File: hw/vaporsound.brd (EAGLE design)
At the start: 100 x 80 mm, 83 parts, among them P9 MA23-2, Q1 BSS138, Q2 BSS138

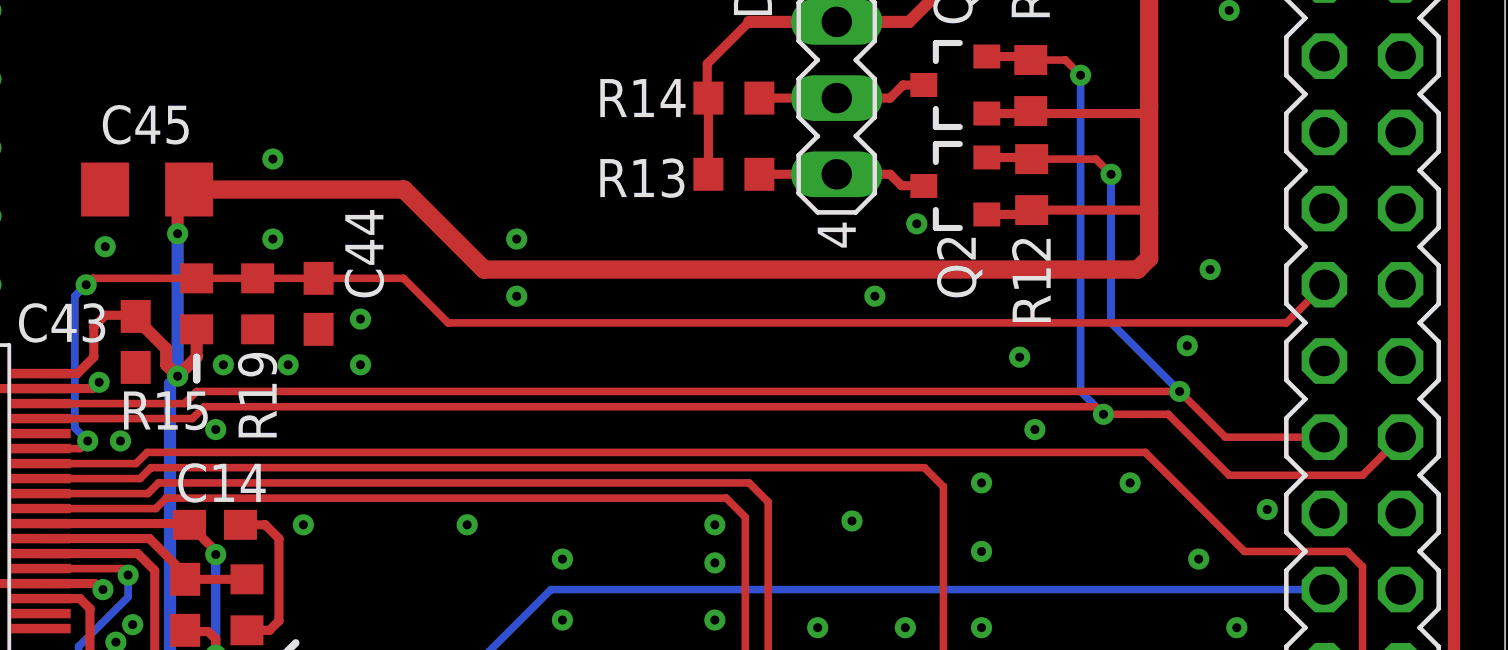
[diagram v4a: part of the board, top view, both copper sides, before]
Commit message: move reset to different bbb pin and remove pull-down resistor
reset of the sta350 is now connected to a pin with pull-up on the bbb instead of one with a pull-down
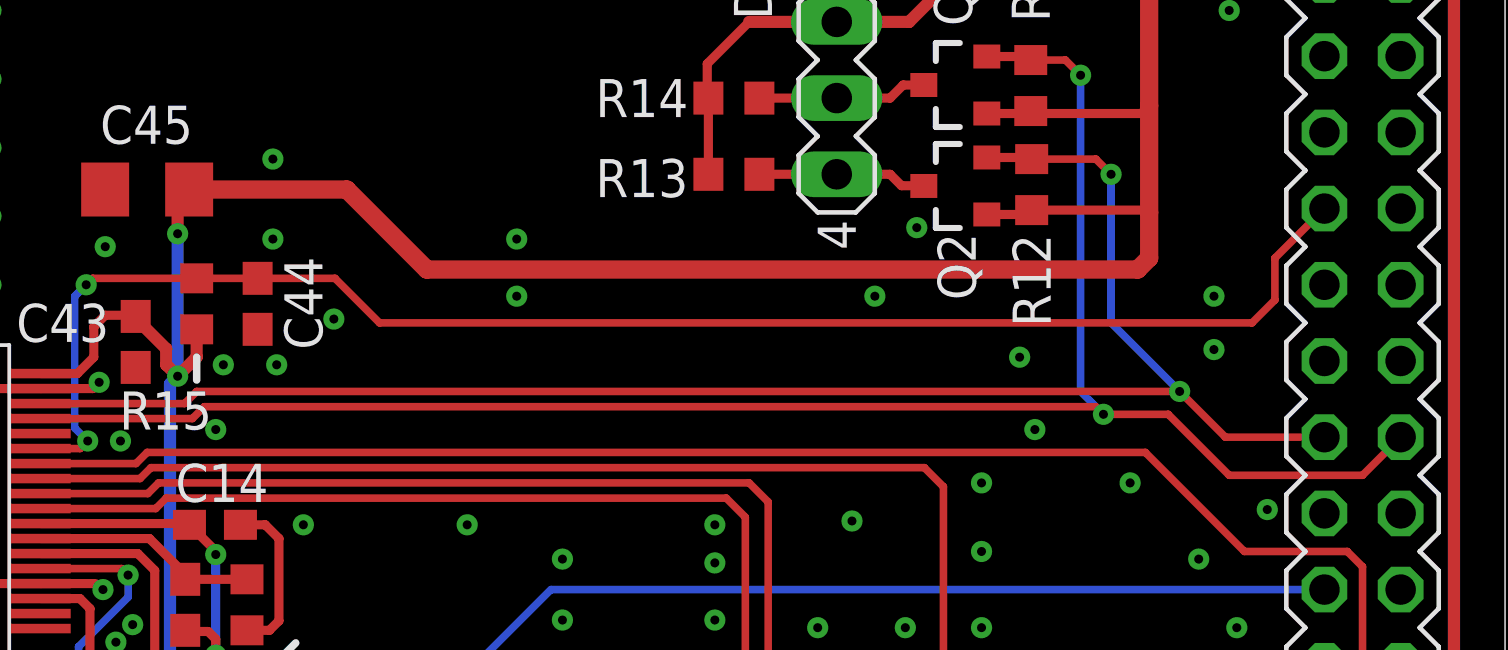
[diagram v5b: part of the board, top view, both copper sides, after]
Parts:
- removed R19: DNP, rcl:R0603
- moved C44 2.03 mm to (58.4, 46.4)
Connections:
- net GND: no longer R19.1
- net RESET: now also P9.13; no longer P9.15, R19.2
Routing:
- net RESET: track 49.8 -> 51.6 mm
- net GND: vias 546 -> 545
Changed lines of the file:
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@@
 <attribute name="VALUE" x="54.483" y="46.99" size="1.27" layer="27" rot="R270"/>
 </element>
-<element name="C44" library="rcl" package="C0603" value="1n" x="60.452" y="46.355" smashed="yes" rot="R270">
-<attribute name="NAME" x="62.611" y="46.482" size="1.27" layer="25" font="vector" ratio="14" rot="R90"/>
-<attribute name="VALUE" x="58.547" y="46.99" size="1.27" layer="27" rot="R270"/>
+<element name="C44" library="rcl" package="C0603" value="1n" x="58.42" y="46.355" smashed="yes" rot="R270">
+<attribute name="NAME" x="60.579" y="44.831" size="1.27" layer="25" font="vector" ratio="14" rot="R90"/>
+<attribute name="VALUE" x="56.515" y="46.99" size="1.27" layer="27" rot="R270"/>
 </element>
 <element name="C45" library="rcl" package="C1206" value="22u" x="54.737" y="50.165" smashed="yes" rot="R180">
@@
 <attribute name="NAME" x="52.0192" y="24.9174" size="1.27" layer="25" font="vector" ratio="14"/>
 <attribute name="VALUE" x="52.9336" y="25.4" size="1.27" layer="27"/>
-</element>
-<element name="R19" library="rcl" package="R0603" value="DNP" x="58.42" y="46.355" smashed="yes" rot="R90">
-<attribute name="NAME" x="57.785" y="44.831" size="1.27" layer="25" font="vector" ratio="14" rot="R270"/>
-<attribute name="VALUE" x="60.325" y="45.72" size="1.27" layer="27" rot="R90"/>
 </element>
 <element name="L1" library="custom-ind" package="SRR1210" value="" x="27.178" y="26.416" smashed="yes">
@@
 <via x="84.328" y="42.164" extent="1-16" drill="0.3"/>
 <via x="57.277" y="44.323" extent="1-16" drill="0.3"/>
-<via x="59.436" y="44.323" extent="1-16" drill="0.3"/>
+<via x="59.055" y="44.323" extent="1-16" drill="0.3"/>
 <via x="83.82" y="44.577" extent="1-16" drill="0.3"/>
-<via x="89.408" y="44.958" extent="1-16" drill="0.3"/>
+<via x="90.297" y="44.831" extent="1-16" drill="0.3"/>
 <via x="80.01" y="28.829" extent="1-16" drill="0.3"/>
 <via x="77.089" y="29.845" extent="1-16" drill="0.3"/>
@@
 <via x="58.928" y="48.514" extent="1-16" drill="0.3"/>
 <via x="78.994" y="46.609" extent="1-16" drill="0.3"/>
-<via x="90.17" y="47.498" extent="1-16" drill="0.3"/>
+<via x="90.297" y="46.609" extent="1-16" drill="0.3"/>
 <via x="82.55" y="32.512" extent="1-16" drill="0.3"/>
 <via x="65.405" y="38.989" extent="1-16" drill="0.3"/>
@@
 <via x="73.66" y="38.989" extent="1-16" drill="0.3"/>
 <contactref element="R18" pad="2"/>
-<contactref element="R19" pad="1"/>
 <via x="78.232" y="39.116" extent="1-16" drill="0.3"/>
 <via x="82.55" y="38.1" extent="1-16" drill="0.3"/>
@@
 <via x="77.724" y="27.2542" extent="1-16" drill="0.3"/>
 <via x="74.168" y="24.003" extent="1-16" drill="0.3"/>
-<via x="61.849" y="44.323" extent="1-16" drill="0.3"/>
 <via x="53.34" y="48.26" extent="1-16" drill="0.3"/>
 <via x="79.121" y="16.002" extent="1-16" drill="0.3"/>
@@
 <via x="88.265" y="29.9974" extent="1-16" drill="0.3"/>
 <via x="58.928" y="51.181" extent="1-16" drill="0.3"/>
-<via x="80.391" y="49.022" extent="1-16" drill="0.3"/>
+<via x="80.391" y="48.895" extent="1-16" drill="0.3"/>
 <via x="20.574" y="67.437" extent="1-16" drill="0.3"/>
 <via x="20.574" y="11.938" extent="1-16" drill="0.3"/>
-<via x="61.849" y="45.847" extent="1-16" drill="0.3"/>
+<via x="60.96" y="45.847" extent="1-16" drill="0.3"/>
 <via x="67.056" y="48.514" extent="1-16" drill="0.3"/>
 <via x="67.056" y="46.609" extent="1-16" drill="0.3"/>
@@
 <wire x1="84.222" y1="49.479" x2="88.062" y2="49.479" width="0.3048" layer="1"/>
 <wire x1="88.062" y1="49.479" x2="88.138" y2="49.403" width="0.3048" layer="1"/>
-<wire x1="65.9638" y1="47.498" x2="87.757" y2="47.498" width="0.6096" layer="1"/>
+<wire x1="64.0588" y1="47.498" x2="87.757" y2="47.498" width="0.6096" layer="1"/>
 <wire x1="87.757" y1="47.498" x2="88.138" y2="47.879" width="0.6096" layer="1"/>
 <wire x1="88.138" y1="47.879" x2="88.138" y2="49.403" width="0.6096" layer="1"/>
@@
 <wire x1="53.34" y1="45.974" x2="54.317" y2="45.974" width="0.3048" layer="1"/>
 <wire x1="54.317" y1="45.974" x2="54.356" y2="45.935" width="0.3048" layer="1"/>
-<wire x1="65.9638" y1="47.498" x2="63.2968" y2="50.165" width="0.6096" layer="1"/>
-<wire x1="56.137" y1="50.165" x2="63.2968" y2="50.165" width="0.6096" layer="1"/>
+<wire x1="64.0588" y1="47.498" x2="61.3918" y2="50.165" width="0.6096" layer="1"/>
+<wire x1="56.137" y1="50.165" x2="61.3918" y2="50.165" width="0.6096" layer="1"/>
 <wire x1="53.848" y1="30.734" x2="52.7694" y2="30.734" width="0.3048" layer="1"/>
 <wire x1="52.7694" y1="30.734" x2="52.7304" y2="30.695" width="0.3048" layer="1"/>
@@
 <signal name="RESET">
 <contactref element="U$1" pad="P$31"/>
-<contactref element="P9" pad="15"/>
 <wire x1="51.191" y1="41.53" x2="52.5028" y2="41.53" width="0.254" layer="1"/>
 <wire x1="52.5028" y1="41.53" x2="52.7558" y2="41.783" width="0.254" layer="1"/>
@@
 <wire x1="52.324" y1="46.609" x2="52.705" y2="46.99" width="0.254" layer="16"/>
 <via x="52.705" y="46.99" extent="1-16" drill="0.3"/>
-<wire x1="64.77" y1="45.72" x2="63.285" y2="47.205" width="0.254" layer="1"/>
-<wire x1="64.77" y1="45.72" x2="92.71" y2="45.72" width="0.254" layer="1"/>
-<wire x1="92.71" y1="45.72" x2="93.98" y2="46.99" width="0.254" layer="1"/>
+<wire x1="62.484" y1="45.72" x2="60.999" y2="47.205" width="0.254" layer="1"/>
+<wire x1="62.484" y1="45.72" x2="91.567" y2="45.72" width="0.254" layer="1"/>
 <contactref element="C44" pad="1"/>
 <contactref element="R15" pad="1"/>
-<contactref element="R19" pad="2"/>
-<wire x1="58.42" y1="47.244" x2="58.42" y2="47.205" width="0.4064" layer="1"/>
-<wire x1="58.42" y1="47.205" x2="60.452" y2="47.205" width="0.254" layer="1"/>
-<wire x1="60.452" y1="47.205" x2="63.285" y2="47.205" width="0.254" layer="1"/>
+<wire x1="58.42" y1="47.205" x2="60.999" y2="47.205" width="0.254" layer="1"/>
 <wire x1="52.705" y1="46.99" x2="52.92" y2="47.205" width="0.254" layer="1"/>
 <wire x1="52.92" y1="47.205" x2="56.388" y2="47.205" width="0.254" layer="1"/>
 <wire x1="56.388" y1="47.205" x2="58.42" y2="47.205" width="0.254" layer="1"/>
+<contactref element="P9" pad="13"/>
+<wire x1="93.98" y1="49.53" x2="92.329" y2="47.879" width="0.254" layer="1"/>
+<wire x1="92.329" y1="47.879" x2="92.329" y2="46.482" width="0.254" layer="1"/>
+<wire x1="92.329" y1="46.482" x2="91.567" y2="45.72" width="0.254" layer="1"/>
 </signal>
 <signal name="POWERDOWN">

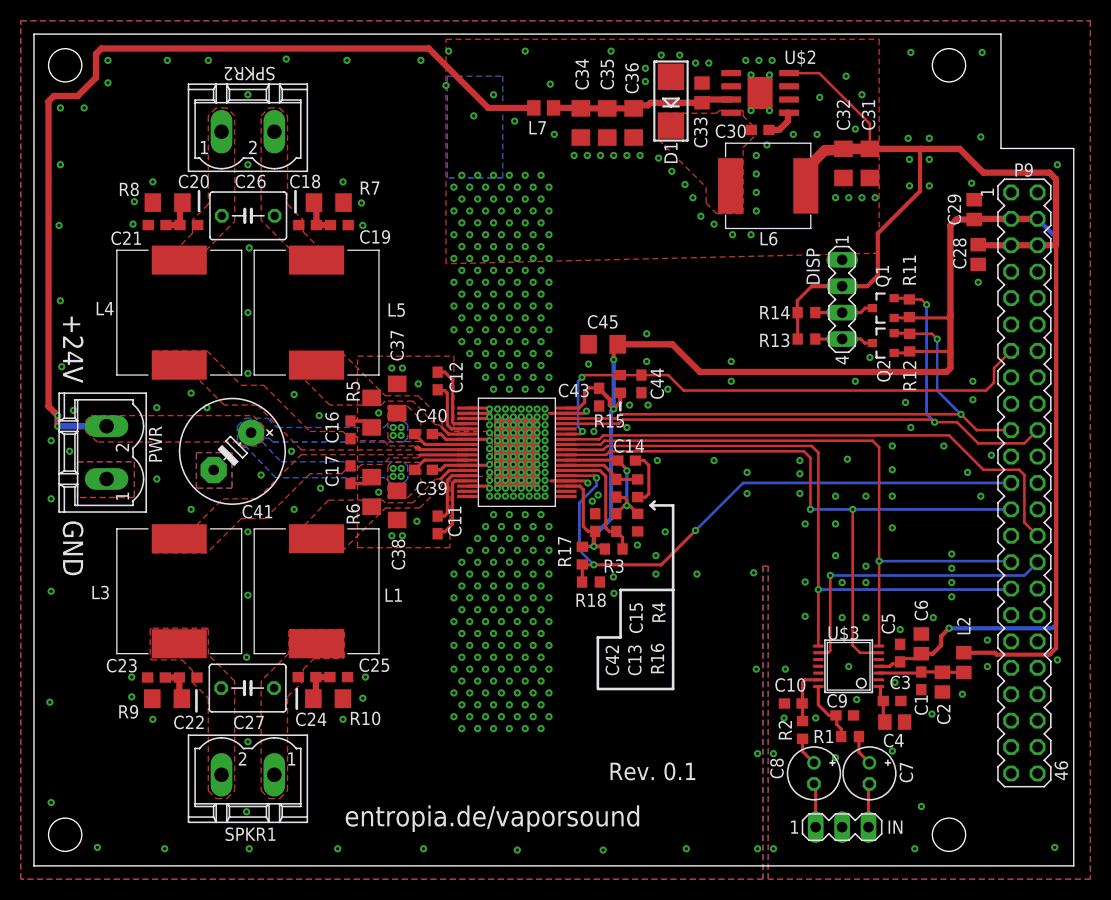
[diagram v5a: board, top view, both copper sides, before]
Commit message: remove soldermask and move some passives to be able to solder a heatsink to the board
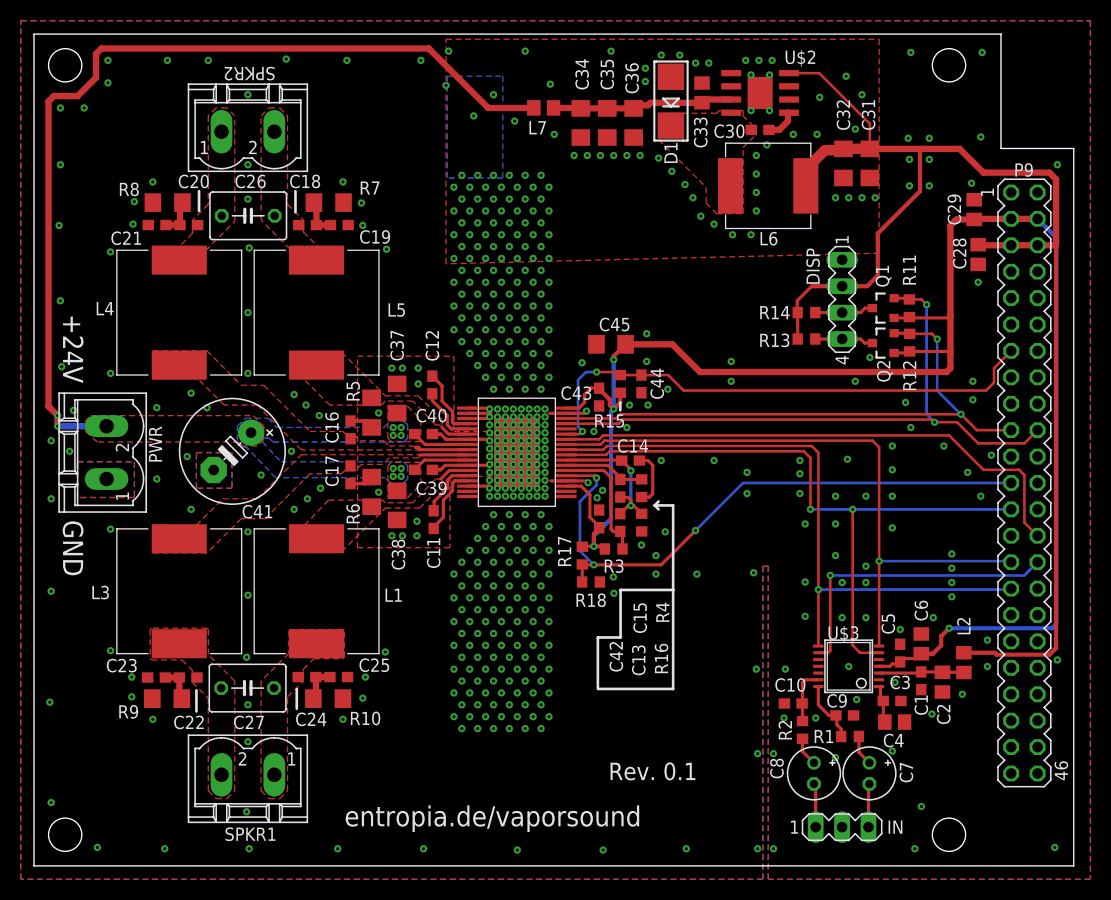
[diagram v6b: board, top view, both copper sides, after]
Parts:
- moved C45 0.76 mm to (55.5, 50.2)
- moved C11 0.63 mm to (38.4, 33.3)
- moved C12 0.63 mm to (38.3, 46.3)
- moved C42 0.52 mm to (54.4, 33.4)
- moved C13 0.38 mm to (56.4, 33.0)
- moved C14 0.38 mm to (57.4, 39.0)
- moved C15 0.38 mm to (56.4, 36.3)
- moved R16 0.38 mm to (58.4, 33.0)
- moved R4 0.38 mm to (58.4, 36.3)
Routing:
- net GND_REG: track 6.34 -> 5.60 mm
- net VDD: track 7.28 -> 6.65 mm
- net +3V3: track 165.5 -> 164.9 mm
- net VSS: track 7.31 -> 6.73 mm
- net VCC_REG: track 6.21 -> 5.69 mm
- net GND: vias 545 -> 558

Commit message: add 1wire temperature sensor + some thermal optimizations
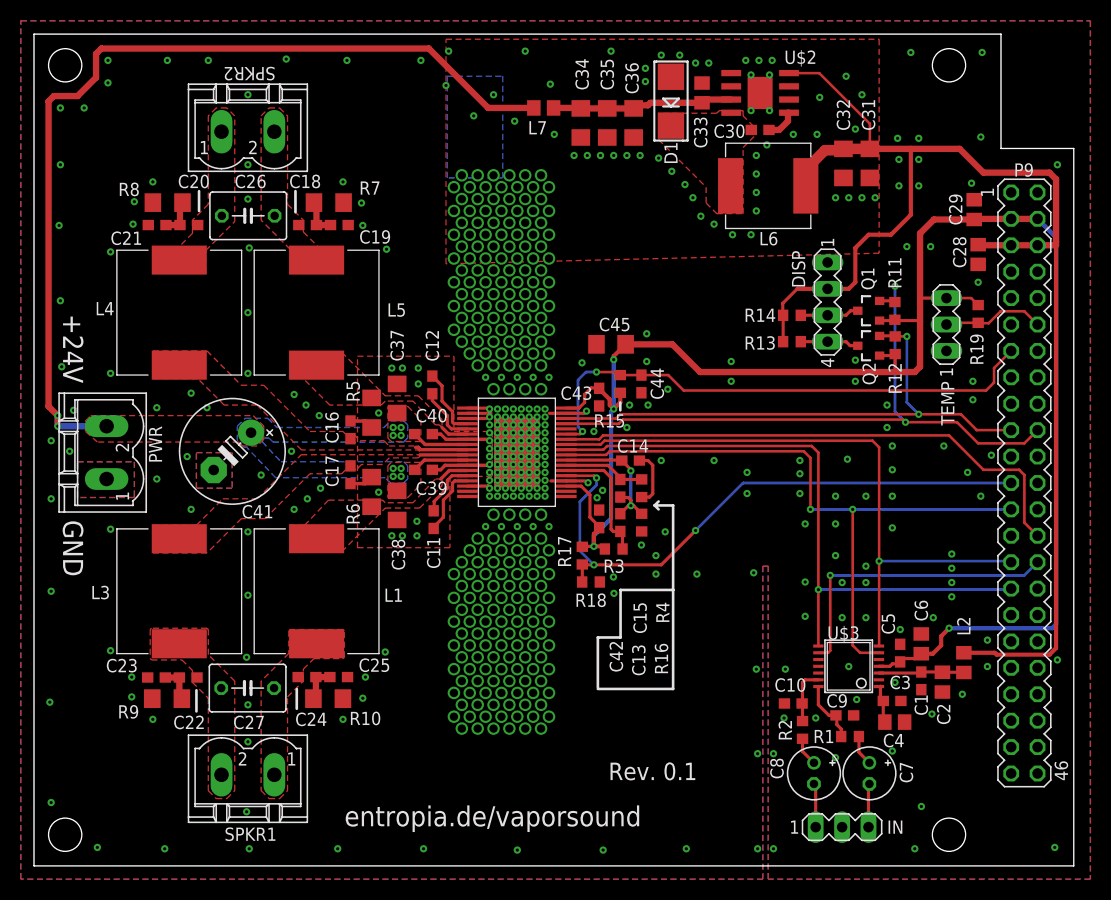
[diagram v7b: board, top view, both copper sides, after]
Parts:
- added R19: 4k7, rcl:R0603
- added TEMP: (no value), con-lstb:MA03-1
- moved R13 1.42 mm to (72.9, 50.4)
- moved DISP 1.42 mm to (76.3, 54.2)
- moved Q1 1.42 mm to (80.3, 53.4)
- moved Q2 1.42 mm to (80.3, 50.0)
- moved R14 1.42 mm to (72.9, 53.0)
- moved R11 1.42 mm to (82.8, 53.4)
- moved R12 1.42 mm to (82.8, 50.1)
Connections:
- new net 1WIRE: P9.12, R19.1, TEMP.2
- net +3V3: now also R19.2, TEMP.3
- net GND: now also TEMP.1
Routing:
- net 1WIRE: track 0.00 -> 9.85 mm
- net SCL: track 56.1 -> 54.2 mm
- net +3V3: track 164.9 -> 166.5 mm
- net +5V: track 128.5 -> 129.9 mm
- net GND: vias 558 -> 560
